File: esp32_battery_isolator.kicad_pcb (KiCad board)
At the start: 4 copper layers, 67.8 x 59.3 mm, 67 parts, among them J1 BATT1, J2 Conn_01x04_Female, J3 USB_B_Micro, J4 BATT2, J5 LOAD1, J6 CHGR, J7 LOAD2, J8 LOAD3, Q10 AP6679GH-HF, Q2 AP6679GH-HF, Q4 AP6679GH-HF, Q6 AP6679GH-HF, Q8 AP6679GH-HF, SW1 C492887, SW2 C492887, SW3 C492887, U1 ESP32-WROOM-32D, U2 LM317AG-TN3-R, U3 ADC128D818, U4 CC6903SO-30A, U5 CH330N, U6 CC6903SO-30A

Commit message: WIP
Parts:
- added D5: SS52, Diode_SMD:D_SMB, F.Cu at (118.7, 80.5)
- added D6: SS52, Diode_SMD:D_SMB, F.Cu at (135.9, 104.1)
- added D7: 1N4148WS, Diode_SMD:D_SOD-323, F.Cu at (135.2, 116.2)
- added D8: 1N4148WS, Diode_SMD:D_SOD-323, F.Cu at (153.1, 116.0)
- added D9: 1N4148WS, Diode_SMD:D_SOD-323, F.Cu at (168.6, 116.0)
- added Q1: MMBT3904, Package_TO_SOT_SMD:SOT-23, F.Cu at (119.7, 76.8)
- added Q3: MMBT3904, Package_TO_SOT_SMD:SOT-23, F.Cu at (136.0, 112.8)
- added Q5: MMBT3904, Package_TO_SOT_SMD:SOT-23, F.Cu at (134.8, 108.1)
- added Q7: MMBT3904, Package_TO_SOT_SMD:SOT-23, F.Cu at (154.1, 110.8)
- added Q9: MMBT3904, Package_TO_SOT_SMD:SOT-23, F.Cu at (158.6, 114.8)
- moved R10 3.46 mm to (116.0, 77.3), turned to 180 degrees
- moved R4 1.87 mm to (139.7, 101.8)
- moved R11 1.76 mm to (116.0, 75.9), turned to 0 degrees
- moved R9 0.32 mm to (165.6, 105.0)
- turned R20 to 90 degrees
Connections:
- D1 pad 2: SYS_OK_LED -> B1_LED
- D3 pad 2: B1_LED -> SYS_OK_LED
- Q10 pad 1: L3ON -> Net-(Q10-Pad1)
- Q2 pad 1: L1ON -> Net-(Q2-Pad1)
- Q4 pad 1: B1ON -> Net-(Q1-Pad3)
- Q6 pad 1: B2ON -> Net-(Q5-Pad3)
- Q8 pad 1: L2ON -> Net-(Q7-Pad3)
- R14 pad 2: B1ON -> Net-(Q1-Pad3)
- R15 pad 2: B2ON -> Net-(Q5-Pad3)
- R16 pad 2: L1ON -> Net-(Q2-Pad1)
- R17 pad 2: L2ON -> Net-(Q7-Pad3)
- R20 pad 2: L3ON -> Net-(Q10-Pad1)
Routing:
- net B2CVD: track 64.0 -> 112.4 mm
- net B2ON: track 22.4 -> 61.8 mm
- net +3V3: track 48.5 -> 86.5 mm, vias 39 -> 35
- net B1C: track 0.00 -> 37.0 mm, vias 19 -> 24
- net COM: track 0.00 -> 30.3 mm, vias 20 -> 25
- net RXD: track 33.4 -> 56.0 mm
- net TXD: track 35.2 -> 51.7 mm
- net L2ON: track 33.4 -> 48.1 mm
- net L1ON: track 46.5 -> 60.2 mm
- net Net-(Q1-Pad3): track 0.00 -> 13.1 mm
- net B2VM: track 151.3 -> 164.2 mm, vias 3 -> 21
- net BOOT: track 13.3 -> 25.2 mm
- net B1ON: track 19.4 -> 29.6 mm
- net Net-(Q10-Pad1): track 0.00 -> 10.1 mm
- net GND: track 67.8 -> 73.3 mm, vias 61 -> 70
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- added copper zone on In2.Cu, net B1C
- added copper zone on In2.Cu, net B1VM
- added copper zone on In2.Cu, net B2C
- added copper zone on In2.Cu, net B2VM
- added copper zone on In2.Cu, net COM
- added copper zone on In2.Cu, net LOAD1
- added copper zone on In2.Cu, net LOAD2
- added copper zone on In2.Cu, net LOAD3

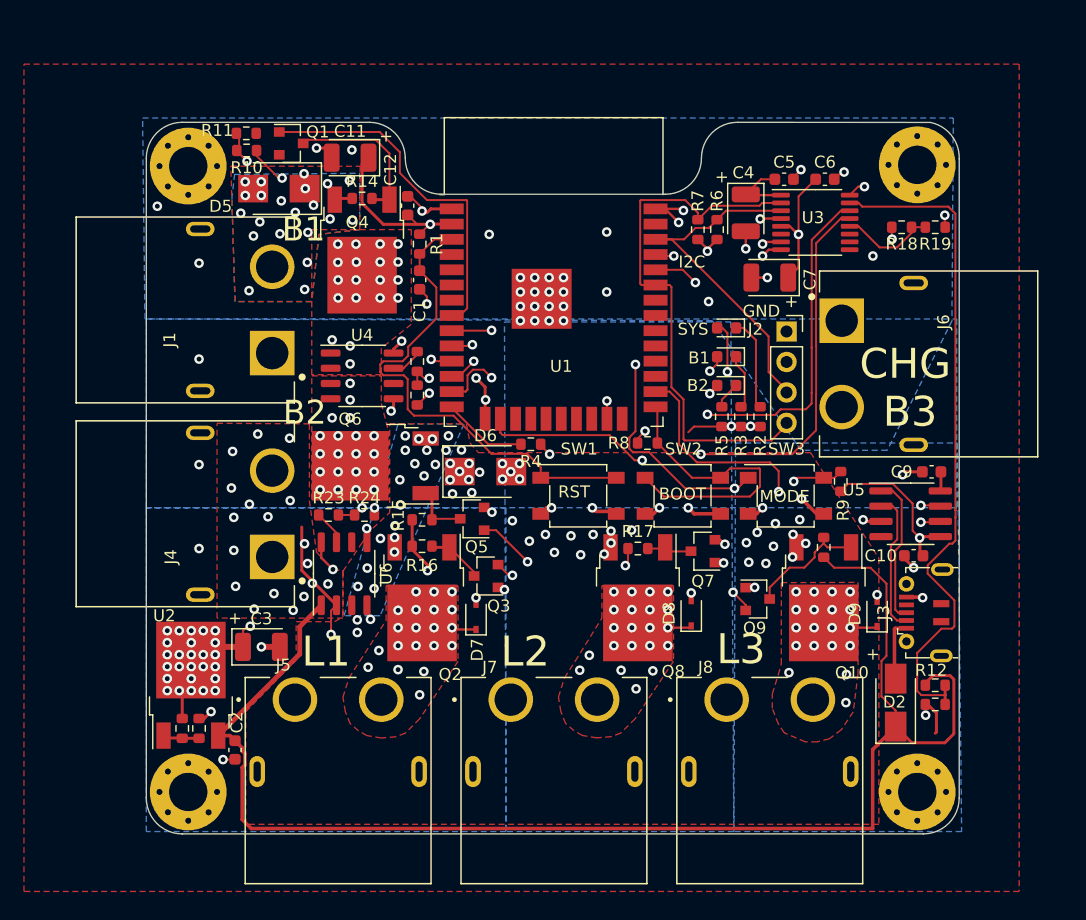
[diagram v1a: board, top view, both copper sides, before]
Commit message: REV D Complete - Off to JLCPCB for assembly!
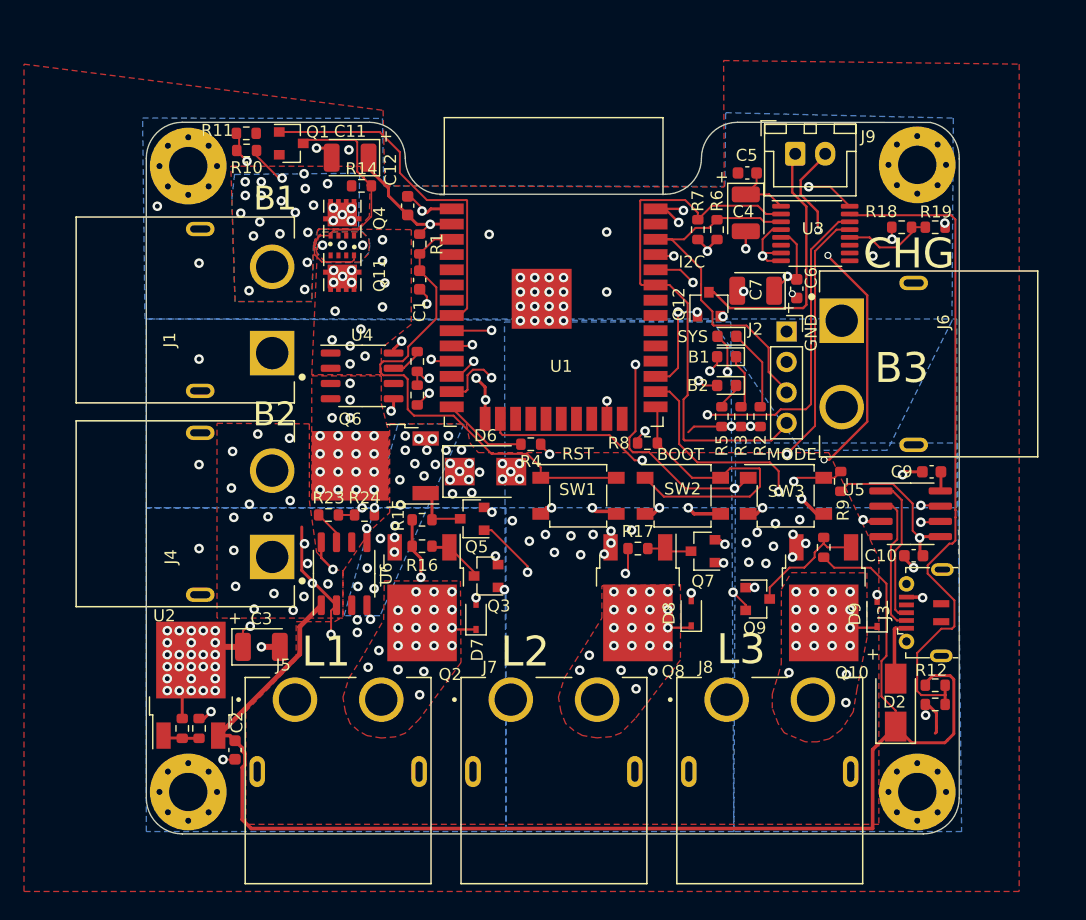
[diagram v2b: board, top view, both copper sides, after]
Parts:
- removed D5: SS52, Diode_SMD:D_SMB
- added J9: Conn_01x02_Male, Connector_JST:JST_XH_B2B-XH-A_1x02_P2.50mm_Vertical, F.Cu at (161.8, 77.6)
- added Q11: AP6679GH, Acea:TRANS_AONR21321, F.Cu at (124.0, 87.5)
- added Q12: MMBT3904, Package_TO_SOT_SMD:SOT-23, F.Cu at (154.6, 90.2)
- Q4: value AP6679GH-HF -> AP6679GH; footprint Package_TO_SOT_SMD:TO-252-2 -> Acea:TRANS_AONR21321
- moved C6 9.42 mm to (161.9, 88.9), turned to 270 degrees
- moved C5 3.12 mm to (157.8, 79.2), turned to 180 degrees
- moved Q4 3.08 mm to (124.0, 83.0), turned to 90 degrees
- moved C7 1.61 mm to (158.5, 89.0)
- moved R14 1.05 mm to (125.6, 80.3)
- moved U3 0.93 mm to (163.4, 84.3)
- moved D1 0.70 mm to (156.1, 92.8)
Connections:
- J3 pad 4: (no net) -> Net-(J3-Pad4)
- Q4 pad 2: B1C -> Net-(Q11-Pad2)
- U1 pad 17: (no net) -> Net-(U1-Pad17)
- U1 pad 18: (no net) -> Net-(U1-Pad18)
- U1 pad 19: (no net) -> Net-(U1-Pad19)
- U1 pad 20: (no net) -> Net-(U1-Pad20)
- U1 pad 21: (no net) -> Net-(U1-Pad21)
- U1 pad 22: (no net) -> Net-(U1-Pad22)
- U1 pad 24: (no net) -> Net-(U1-Pad24)
- U1 pad 27: (no net) -> FANON
- U1 pad 28: (no net) -> Net-(U1-Pad28)
- U1 pad 29: (no net) -> Net-(U1-Pad29)
- U1 pad 30: (no net) -> Net-(U1-Pad30)
- U1 pad 31: (no net) -> Net-(U1-Pad31)
- U1 pad 32: (no net) -> Net-(U1-Pad32)
- U1 pad 37: (no net) -> Net-(U1-Pad37)
- U1 pad 4: (no net) -> Net-(U1-Pad4)
- U1 pad 5: (no net) -> Net-(U1-Pad5)
- U1 pad 6: (no net) -> Net-(U1-Pad6)
- U1 pad 7: (no net) -> Net-(U1-Pad7)
- U3 pad 10: (no net) -> Net-(U3-Pad10)
- U3 pad 11: (no net) -> Net-(U3-Pad11)
- U3 pad 6: (no net) -> Net-(U3-Pad6)
- U3 pad 9: (no net) -> Net-(U3-Pad9)
- U4 pad 6: (no net) -> Net-(U4-Pad6)
- U5 pad 4: (no net) -> Net-(U5-Pad4)
- U6 pad 6: (no net) -> Net-(U6-Pad6)
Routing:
- net B2C: track 0.00 -> 30.4 mm, vias 52 -> 55
- net FANGND: track 0.00 -> 22.0 mm
- net B2CVD: track 112.4 -> 96.4 mm
- net B1C: track 37.0 -> 25.2 mm, vias 24 -> 20
- net Net-(Q1-Pad3): track 13.1 -> 22.2 mm
- net FANON: track 0.00 -> 8.43 mm, vias 0 -> 2
- net +3V3: track 86.5 -> 79.1 mm
- net GND: track 73.3 -> 69.9 mm, vias 70 -> 67
- net B1_LED: track 32.6 -> 30.1 mm
- net B1VD: track 57.6 -> 55.5 mm
- net RXD: track 56.0 -> 54.0 mm
- net B1VM: track 4.71 -> 3.21 mm, vias 17 -> 19
- net SCL: track 29.6 -> 31.1 mm
- net SYS_OK_LED: track 28.4 -> 27.0 mm
- net Net-(D1-Pad1): track 7.78 -> 6.84 mm
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- added copper zone on B.Cu, net Net-(Q11-Pad2)
- added copper zone on F.Cu, net Net-(Q11-Pad2)
- removed copper zone on In2.Cu, net B1C
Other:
- net class Default: clearance 0.2 -> 0.17
- rule trace_clearance: 0.2 -> 0.17
- rule trace_min: 0.167 -> 0.127
- board text added: "BATTERY ISOLATOR LITE REV.D ACEA QUIGG 04/20"
- board text removed: "BATTERY ISOLATOR LITE REV.D ACEA QUIGG 02/20"

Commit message: committing
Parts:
- removed C3: 1uF, Capacitor_Tantalum_SMD:CP_EIA-3528-21_Kemet-B
- removed D4: MAIN LED, LED_SMD:LED_0603_1608Metric
- removed D6: SS52, Diode_SMD:D_SMB
- removed D7: 1N4148WS, Diode_SMD:D_SOD-323
- removed the J5 at (123.7, 123.2)
- removed R25: 200R, Resistor_SMD:R_0603_1608Metric
- removed R26: 330R, Resistor_SMD:R_0603_1608Metric
- removed R5: 3.6k, Resistor_SMD:R_0603_1608Metric
- removed SW3: C492887, Acea:TS4550TP
- removed U2: LM317AG-TN3-R, Package_TO_SOT_SMD:TO-252-2
- added C13: 100n, Capacitor_SMD:C_0603_1608Metric, F.Cu at (119.5, 79.6)
- added C14: 10u, Capacitor_SMD:C_0805_2012Metric, F.Cu at (126.7, 80.2)
- added C15: 4.7u, Capacitor_SMD:C_0805_2012Metric, F.Cu at (128.7, 81.2)
- added C8: 4.7, Capacitor_SMD:C_0805_2012Metric, F.Cu at (116.0, 81.0)
- added J7: LOAD2, Acea:AMASS_XT60PW-F, F.Cu at (159.7, 123.1)
- added L1: L_Small, Inductor_SMD:L_Taiyo-Yuden_NR-30xx, F.Cu at (123.7, 81.5)
- added Q13: AONR21321, Acea:TRANS_AONR21321, F.Cu at (128.9, 99.9)
- added R27: 510R, Resistor_SMD:R_0603_1608Metric, F.Cu at (130.1, 90.2)
- added R28: 510R, Resistor_SMD:R_0603_1608Metric, F.Cu at (133.2, 118.8)
- added R29: 510R, Resistor_SMD:R_0603_1608Metric, F.Cu at (135.9, 105.2)
- added R30: 510R, Resistor_SMD:R_0603_1608Metric, F.Cu at (151.1, 118.8)
- added R31: 510R, Resistor_SMD:R_0603_1608Metric, F.Cu at (168.2, 99.8)
- added U7: BL9342, Package_TO_SOT_SMD:SOT-23-6, F.Cu at (119.0, 77.0)
- C11: value 1uF -> 33p; footprint Capacitor_Tantalum_SMD:CP_EIA-3528-21_Kemet-B -> Capacitor_SMD:C_0603_1608Metric
- D1, D3: value MAIN LED -> B5819W; footprint LED_SMD:LED_0603_1608Metric -> Diode_SMD:D_SOD-123
- D2: value SS14 -> B5819W; footprint Diode_SMD:D_SMA -> Diode_SMD:D_SOD-123
- D8, D9: value 1N4148WS -> B5819W; footprint Diode_SMD:D_SOD-323 -> Diode_SMD:D_SOD-123
- J5: renamed from J7; value LOAD2 -> LOAD1
- J9: value Conn_01x02_Male -> Conn_01x03_Male; footprint Connector_JST:JST_XH_B2B-XH-A_1x02_P2.50mm_Vertical -> Connector_JST:JST_SH_SM03B-SRSS-TB_1x03-1MP_P1.00mm_Horizontal
- Q10, Q2, Q6, Q8: value AP6679GH-HF -> AONR21321; footprint Package_TO_SOT_SMD:TO-252-2 -> Acea:TRANS_AONR21321
- Q11, Q4: value AP6679GH -> AONR21321
- R2: value 3.6k -> 124k
- R3: value 3.6k -> 40.2k
- moved J6 58.8 mm to (123.7, 129.2), turned to 180 degrees
- moved C2 50.4 mm to (115.8, 77.0), turned to 90 degrees
- moved R10 49.0 mm to (164.9, 79.9), turned to 90 degrees
- moved R11 49.0 mm to (164.9, 76.8), turned to 90 degrees
- moved R13 47.1 mm to (167.6, 76.8), turned to 90 degrees
- moved R23 46.2 mm to (159.7, 79.9), turned to 90 degrees
- moved R24 45.8 mm to (159.7, 76.8), turned to 90 degrees
- moved J9 44.5 mm to (172.4, 120.8), turned to 270 degrees
- moved R12 42.4 mm to (167.6, 80.0), turned to 90 degrees
- moved R3 41.4 mm to (121.8, 78.0)
- moved R2 40.3 mm to (124.8, 78.0)
- moved Q12 39.8 mm to (172.8, 125.5)
- moved D1 38.4 mm to (119.3, 81.8)
- moved R22 38.3 mm to (162.3, 76.8), turned to 90 degrees
- moved D2 37.8 mm to (171.4, 85.7), turned to 0 degrees
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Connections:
- C11 pad 1: +3V3 -> Net-(C11-Pad1)
- C11 pad 2: GND -> +3V3
- D1 pad 1: Net-(D1-Pad1) -> Net-(C13-Pad2)
- D1 pad 2: B1_LED -> GND
- D3 pad 1: Net-(D3-Pad1) -> LOAD1
- D3 pad 2: SYS_OK_LED -> GND
- J3 pad 4: Net-(J3-Pad4) -> (no net)
- J5 pad 2: LOAD2 -> LOAD1
- J9 pad 1: FANGND -> B2C
- J9 pad 2: B2C -> FANGND
- Q1 pad 1: B1ON -> Net-(Q1-Pad1)
- Q3 pad 1: L1ON -> Net-(Q3-Pad1)
- Q5 pad 1: B2ON -> Net-(Q5-Pad1)
- Q6 pad 2: COM -> Net-(Q13-Pad2)
- Q7 pad 1: L2ON -> Net-(Q7-Pad1)
- Q9 pad 1: L3ON -> Net-(Q9-Pad1)
- R2 pad 1: Net-(D1-Pad1) -> Net-(C11-Pad1)
- R2 pad 2: GND -> +3V3
- R3 pad 1: Net-(D3-Pad1) -> Net-(C11-Pad1)
- R9 pad 1: MODE -> BOOT
- U1 pad 10: B2_LED -> B2ON
- U1 pad 11: B2ON -> (no net)
- U1 pad 12: SYS_OK_LED -> (no net)
- U1 pad 13: B1_LED -> L1ON
- U1 pad 17: Net-(U1-Pad17) -> (no net)
- U1 pad 18: Net-(U1-Pad18) -> (no net)
- U1 pad 19: Net-(U1-Pad19) -> (no net)
- U1 pad 20: Net-(U1-Pad20) -> (no net)
- U1 pad 21: Net-(U1-Pad21) -> (no net)
- U1 pad 22: Net-(U1-Pad22) -> (no net)
- U1 pad 23: L1ON -> (no net)
- U1 pad 24: Net-(U1-Pad24) -> (no net)
- U1 pad 28: Net-(U1-Pad28) -> RPM
- U1 pad 29: Net-(U1-Pad29) -> (no net)
- U1 pad 30: Net-(U1-Pad30) -> (no net)
- U1 pad 31: Net-(U1-Pad31) -> (no net)
- U1 pad 32: Net-(U1-Pad32) -> (no net)
- U1 pad 37: Net-(U1-Pad37) -> (no net)
- U1 pad 4: Net-(U1-Pad4) -> (no net)
- U1 pad 5: Net-(U1-Pad5) -> (no net)
- U1 pad 6: Net-(U1-Pad6) -> (no net)
- U1 pad 7: Net-(U1-Pad7) -> (no net)
- U1 pad 9: MODE -> BOOT
- U3 pad 10: Net-(U3-Pad10) -> (no net)
- U3 pad 11: Net-(U3-Pad11) -> (no net)
- U3 pad 6: Net-(U3-Pad6) -> (no net)
- U3 pad 9: Net-(U3-Pad9) -> (no net)
- U4 pad 6: Net-(U4-Pad6) -> (no net)
- U5 pad 4: Net-(U5-Pad4) -> (no net)
- U6 pad 6: Net-(U6-Pad6) -> (no net)
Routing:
- net B2CVD: track 96.4 -> 10.6 mm, vias 2 -> 0
- net RPM: track 0.00 -> 62.7 mm, vias 0 -> 2
- net FANON: track 8.43 -> 62.2 mm, vias 2 -> 0
- net B2CM: track 2.89 -> 54.8 mm, vias 0 -> 2
- net B1VD: track 55.5 -> 5.36 mm, vias 2 -> 0
- net B2VM: track 164.8 -> 214.6 mm, vias 21 -> 13
- net B2ON: track 62.3 -> 13.1 mm, vias 2 -> 0
- net B2VD: track 56.0 -> 6.96 mm
- net B1CM: track 2.69 -> 47.8 mm, vias 0 -> 2
- net B1CVD: track 53.1 -> 8.10 mm, vias 2 -> 0
- net MODE: track 44.8 -> 0.00 mm, vias 4 -> 0
- net B1VM: track 3.21 -> 47.8 mm, vias 19 -> 7
- net L1ON: track 60.2 -> 22.8 mm
- net COM: track 30.3 -> 0.00 mm, vias 25 -> 5
- net B1_LED: track 30.1 -> 0.00 mm, vias 2 -> 0
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- added copper zone on F.Cu, net +3V3
- added copper zone on B.Cu, net B2VM
- added copper zone on F.Cu, net Net-(C13-Pad2)
- added copper zone on B.Cu, net Net-(Q13-Pad2)
- added copper zone on F.Cu, net Net-(Q13-Pad2)
- removed copper zone on In2.Cu, net +3V3
- removed copper zone on In2.Cu, net B1VM
- removed copper zone on In2.Cu, net B2VM
- removed copper zone on In2.Cu, net COM
- removed copper zone on In2.Cu, net LOAD1
- removed copper zone on In2.Cu, net LOAD2
- removed copper zone on In2.Cu, net LOAD3
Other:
- net class Default: via_drill 0.4 -> 0.45
- board text removed: "GND"
- board text removed: "I2C"
- board text removed: "MODE"
- board text removed: "SYS"

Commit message: REV E - shipped to JLCPCB
Good to go for JLCPCB assembly service
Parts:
- added REF**: KiCad-Logo2_5mm_SilkScreen, Symbol:KiCad-Logo2_5mm_SilkScreen, B.Cu at (141.4, 104.3)
- added Ref**: Val**, Acea:aces_electronics_small, F.Cu at (112.0, 121.7)
- C15: value 4.7u -> 4.7uF
- C8: value 4.7 -> 4.7uF
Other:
- board text added: "B3/ CHG"
- board text added: "BATTERY ISOLATOR LITE REV.E ACEA QUIGG 07/21"
- board text removed: "B3"
- board text removed: "BATTERY ISOLATOR LITE REV.D ACEA QUIGG 04/20"
- board text removed: "CHG"

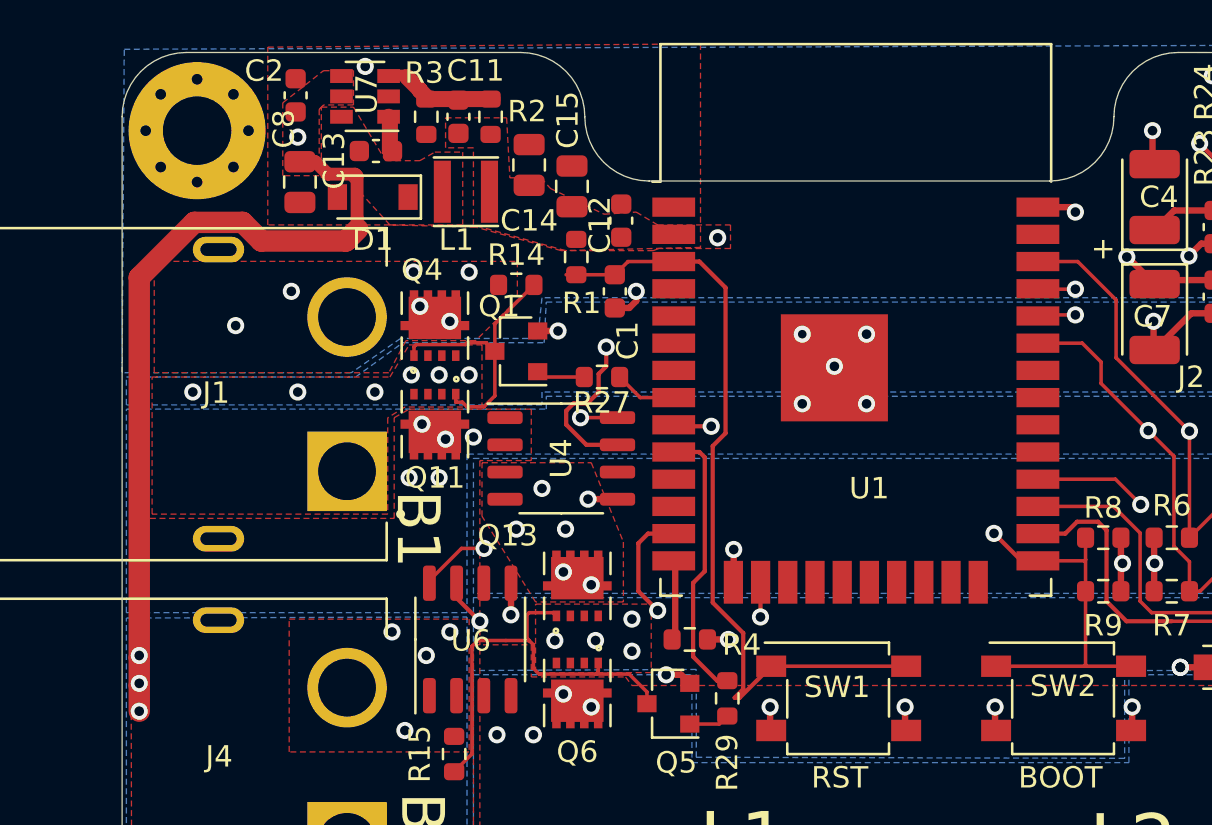
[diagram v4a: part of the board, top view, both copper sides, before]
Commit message: REV F - WIP fixed ground plane issuer around SMPS
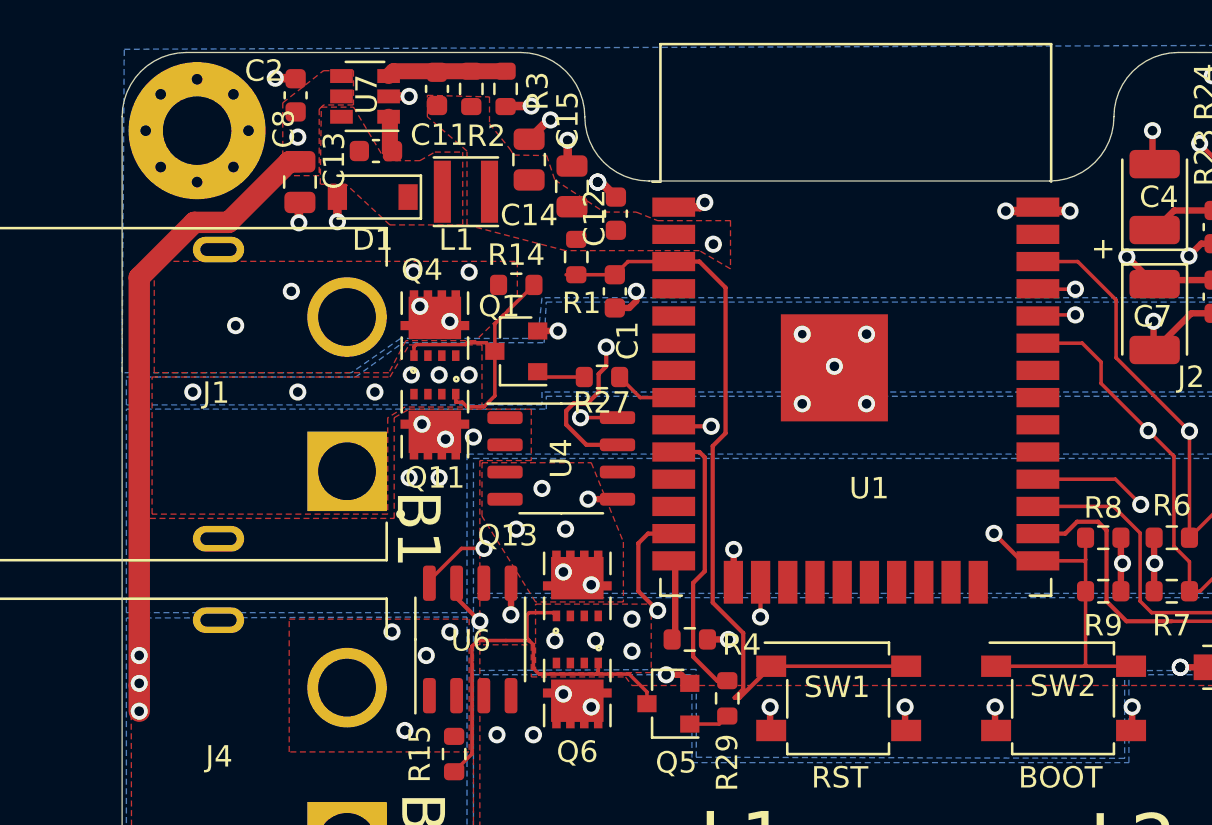
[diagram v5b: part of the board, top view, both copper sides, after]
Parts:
- moved R3 3.92 mm to (125.5, 76.7)
- moved C11 1.64 mm to (122.3, 76.7)
- moved R2 1.58 mm to (124.0, 76.7)
- moved C12 0.41 mm to (130.7, 82.5)
- moved C14 0.25 mm to (126.7, 80.0)
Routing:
- net GND: track 50.7 -> 62.4 mm, vias 39 -> 49
- net B2VM: track 214.6 -> 207.5 mm
- net B2CM: track 54.8 -> 53.7 mm
- removed copper zone on F.Cu, net GND
